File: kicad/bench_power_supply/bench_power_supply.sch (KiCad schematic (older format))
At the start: 0 parts

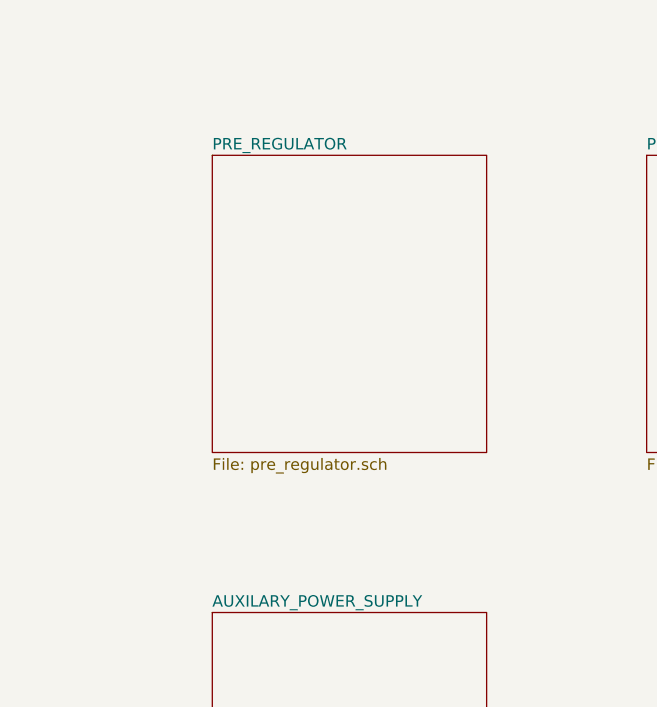
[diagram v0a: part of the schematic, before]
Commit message: Added pre-regulator connector hlabels
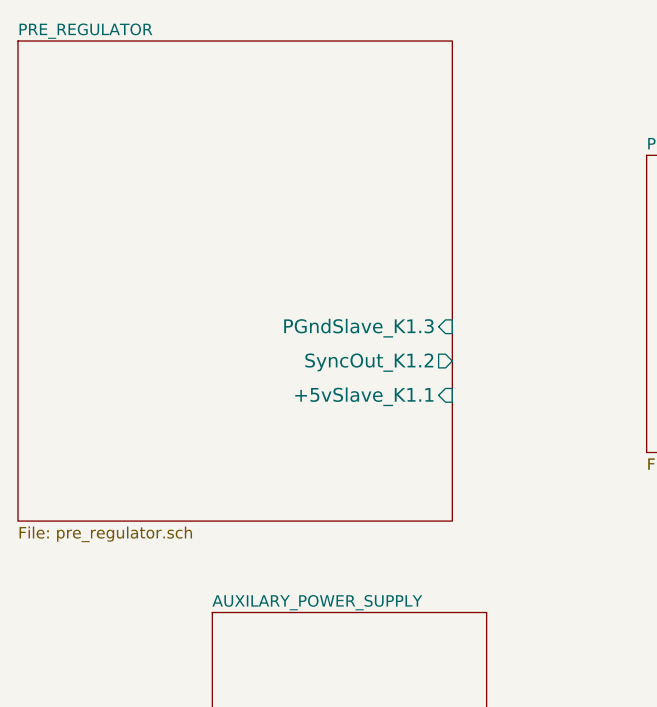
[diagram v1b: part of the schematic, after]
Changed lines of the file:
@@
 Sheet 1 5
 Title "ROOT"
-Date "9 feb 2016"
+Date "15 feb 2016"
 Rev ""
 Comp ""
@@
 Comment4 ""
 $EndDescr
-$Sheet
-S 1700 1150 1200 1300
-U 56BA34F4
-F0 "PRE_REGULATOR" 50
-F1 "pre_regulator.sch" 50
-$EndSheet
 $Sheet
 S 3600 1150 1200 1300
@@
 F1 "digital_control.sch" 50
 $EndSheet
+$Sheet
+S 850  650  1900 2100
+U 56BA34F4
+F0 "PRE_REGULATOR" 50
+F1 "pre_regulator.sch" 50
+F2 "+5vSlave_K1.1" I R 2750 2200 60
+F3 "SyncOut_K1.2" O R 2750 2050 60
+F4 "PGndSlave_K1.3" I R 2750 1900 60
+$EndSheet
 $EndSCHEMATC

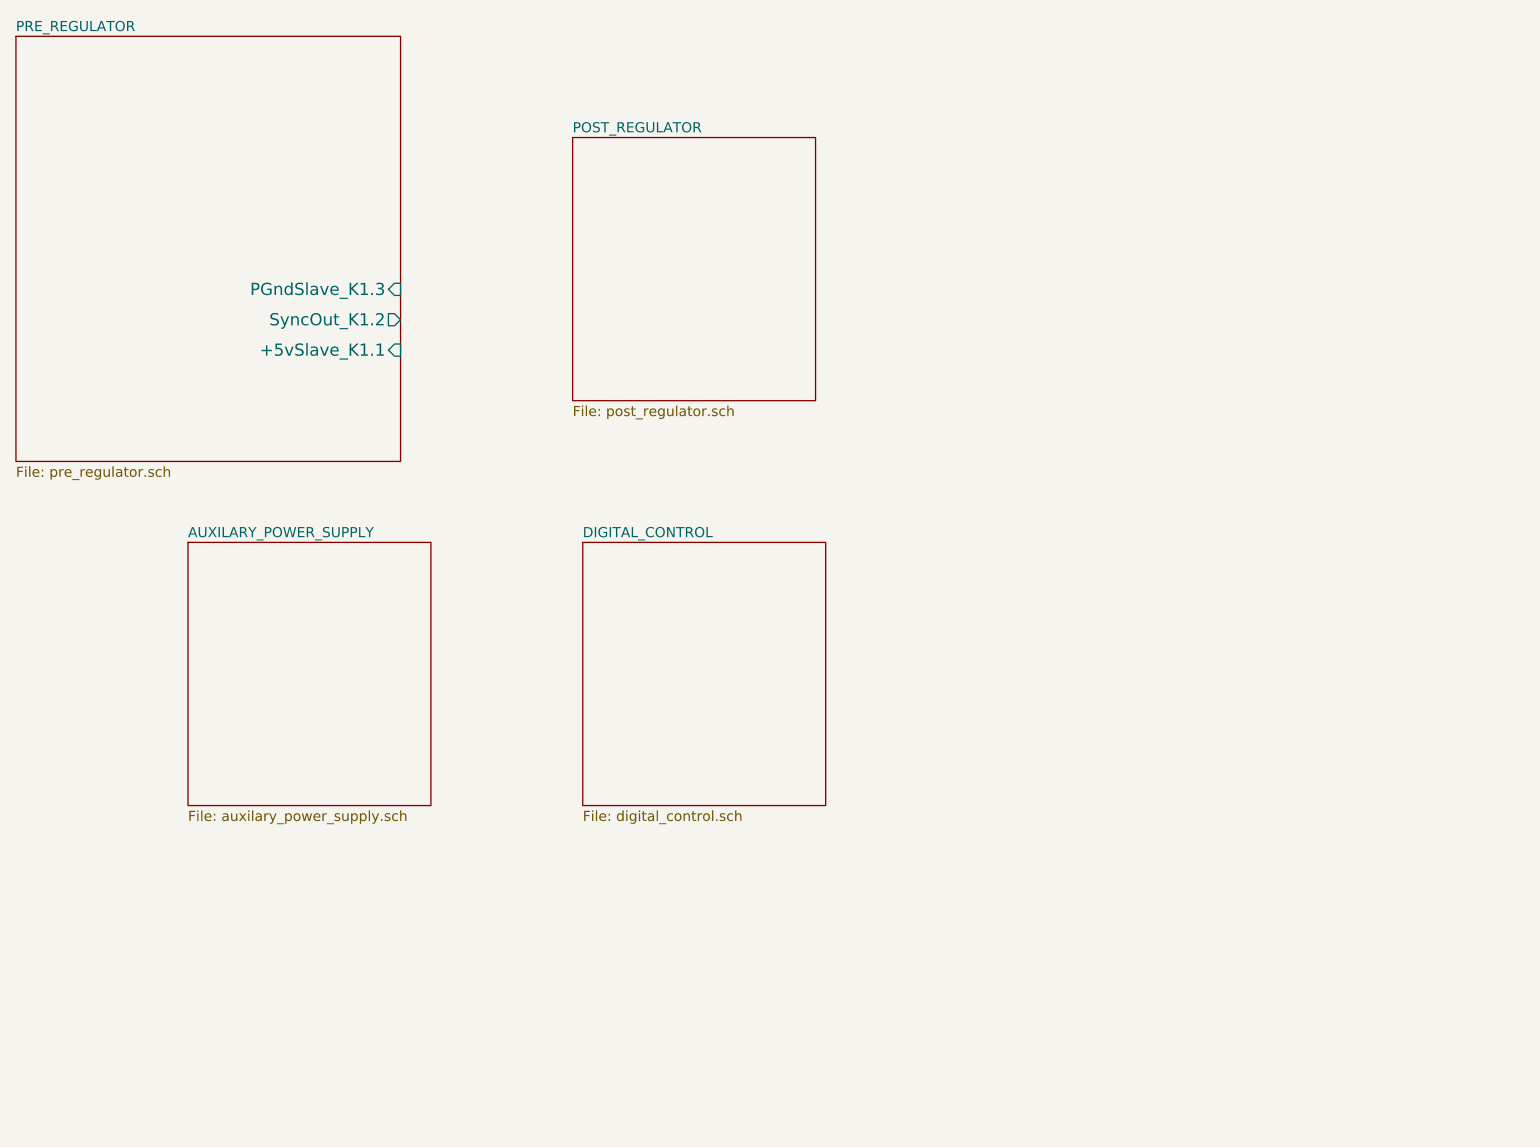
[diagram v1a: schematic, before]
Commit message: Added hlabels to pre-regulator
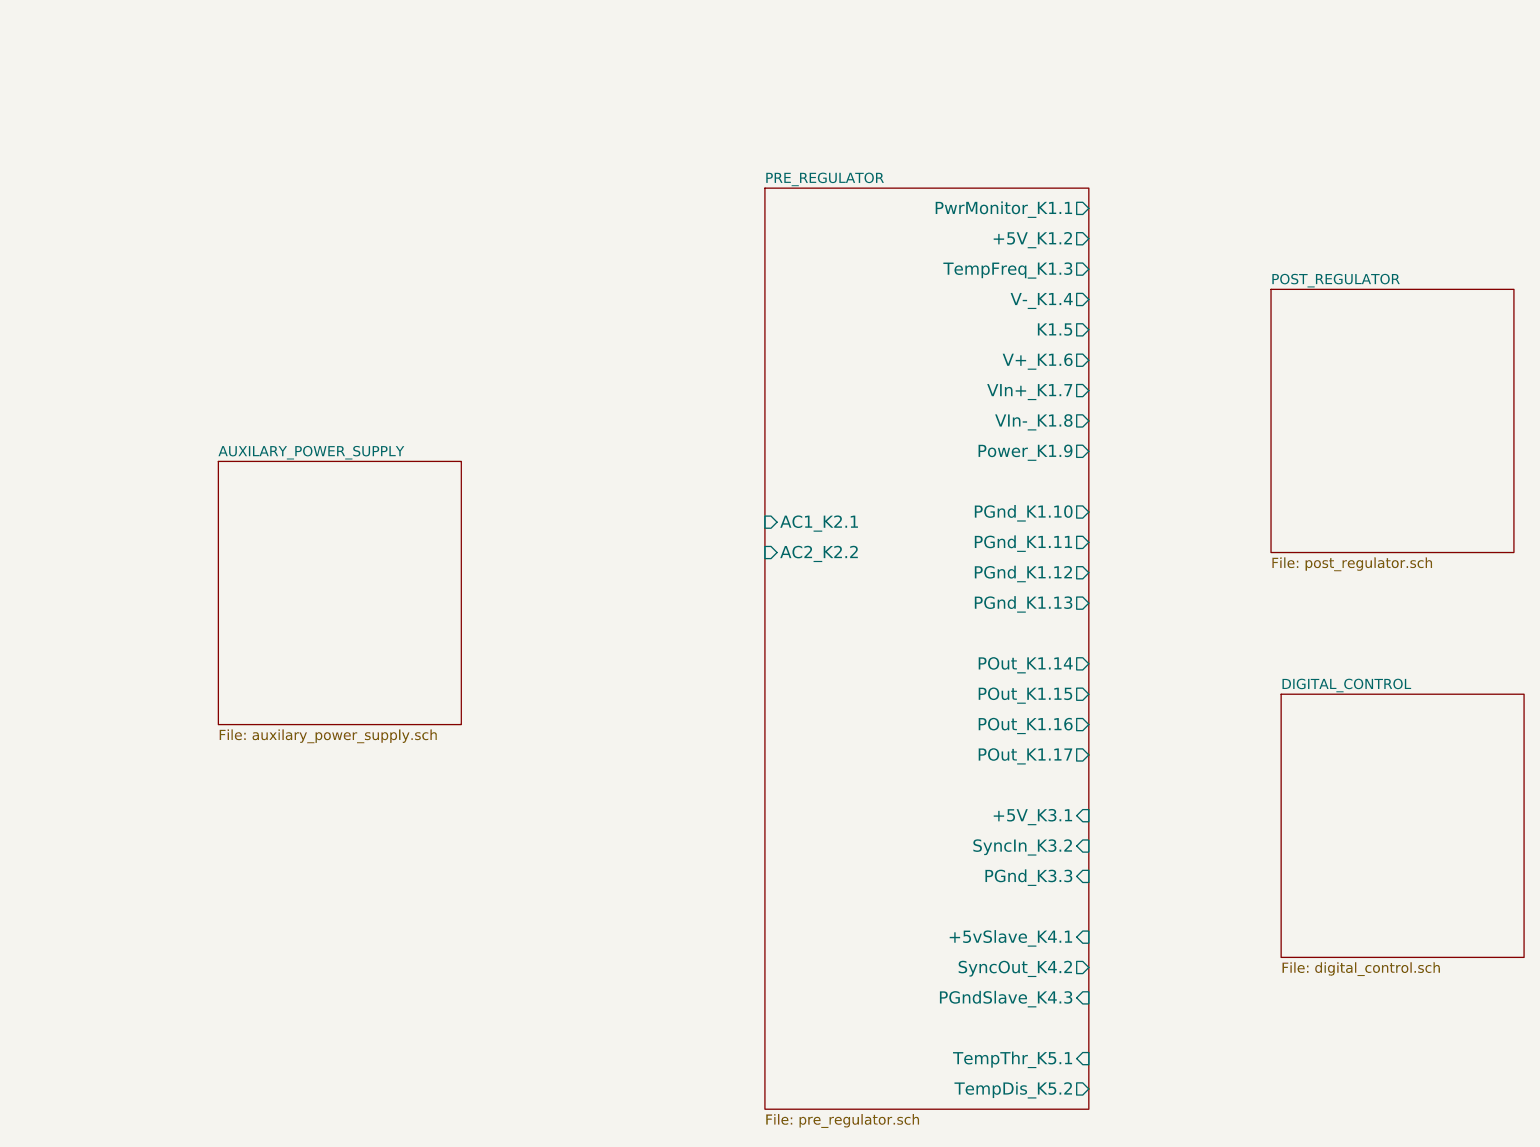
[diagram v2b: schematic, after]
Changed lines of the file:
@@
 $EndDescr
 $Sheet
-S 3600 1150 1200 1300
+S 7050 1900 1200 1300
 U 56BA3538
 F0 "POST_REGULATOR" 50
@@
 $EndSheet
 $Sheet
-S 1700 3150 1200 1300
+S 1850 2750 1200 1300
 U 56BA3567
 F0 "AUXILARY_POWER_SUPPLY" 50
@@
 $EndSheet
 $Sheet
-S 3650 3150 1200 1300
+S 7100 3900 1200 1300
 U 56BA363F
 F0 "DIGITAL_CONTROL" 50
@@
 $EndSheet
 $Sheet
-S 850  650  1900 2100
+S 4550 1400 1600 4550
 U 56BA34F4
 F0 "PRE_REGULATOR" 50
 F1 "pre_regulator.sch" 50
-F2 "+5vSlave_K1.1" I R 2750 2200 60
-F3 "SyncOut_K1.2" O R 2750 2050 60
-F4 "PGndSlave_K1.3" I R 2750 1900 60
+F2 "+5V_K3.1" I R 6150 4500 60
+F3 "SyncIn_K3.2" I R 6150 4650 60
+F4 "PGnd_K3.3" I R 6150 4800 60
+F5 "TempThr_K5.1" I R 6150 5700 60
+F6 "TempDis_K5.2" O R 6150 5850 60
+F7 "+5V_K1.2" O R 6150 1650 60
+F8 "PwrMonitor_K1.1" O R 6150 1500 60
+F9 "TempFreq_K1.3" O R 6150 1800 60
+F10 "POut_K1.15" O R 6150 3900 60
+F11 "POut_K1.14" O R 6150 3750 60
+F12 "POut_K1.17" O R 6150 4200 60
+F13 "POut_K1.16" O R 6150 4050 60
+F14 "PGnd_K1.11" O R 6150 3150 60
+F15 "PGnd_K1.10" O R 6150 3000 60
+F16 "PGnd_K1.13" O R 6150 3450 60
+F17 "PGnd_K1.12" O R 6150 3300 60
+F18 "Power_K1.9" O R 6150 2700 60
+F19 "V-_K1.4" O R 6150 1950 60
+F20 "V+_K1.6" O R 6150 2250 60
+F21 "VIn+_K1.7" O R 6150 2400 60
+F22 "VIn-_K1.8" O R 6150 2550 60
+F23 "+5vSlave_K4.1" I R 6150 5100 60
+F24 "SyncOut_K4.2" O R 6150 5250 60
+F25 "PGndSlave_K4.3" I R 6150 5400 60
+F26 "K1.5" O R 6150 2100 60
+F27 "AC1_K2.1" I L 4550 3050 60
+F28 "AC2_K2.2" I L 4550 3200 60
 $EndSheet
 $EndSCHEMATC

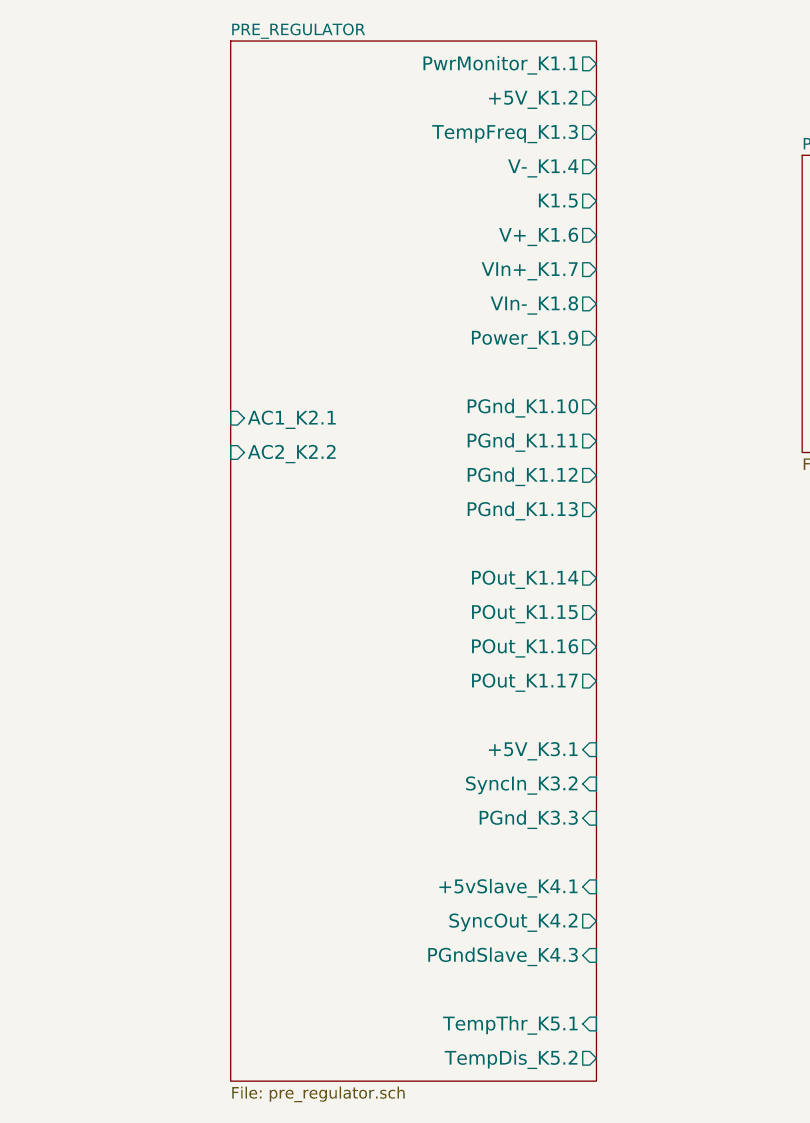
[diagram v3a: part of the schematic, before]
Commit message: Split pre-regulator into two new schemas. Previous pre_regulator.sch has been renamed to pre_regulator_module.
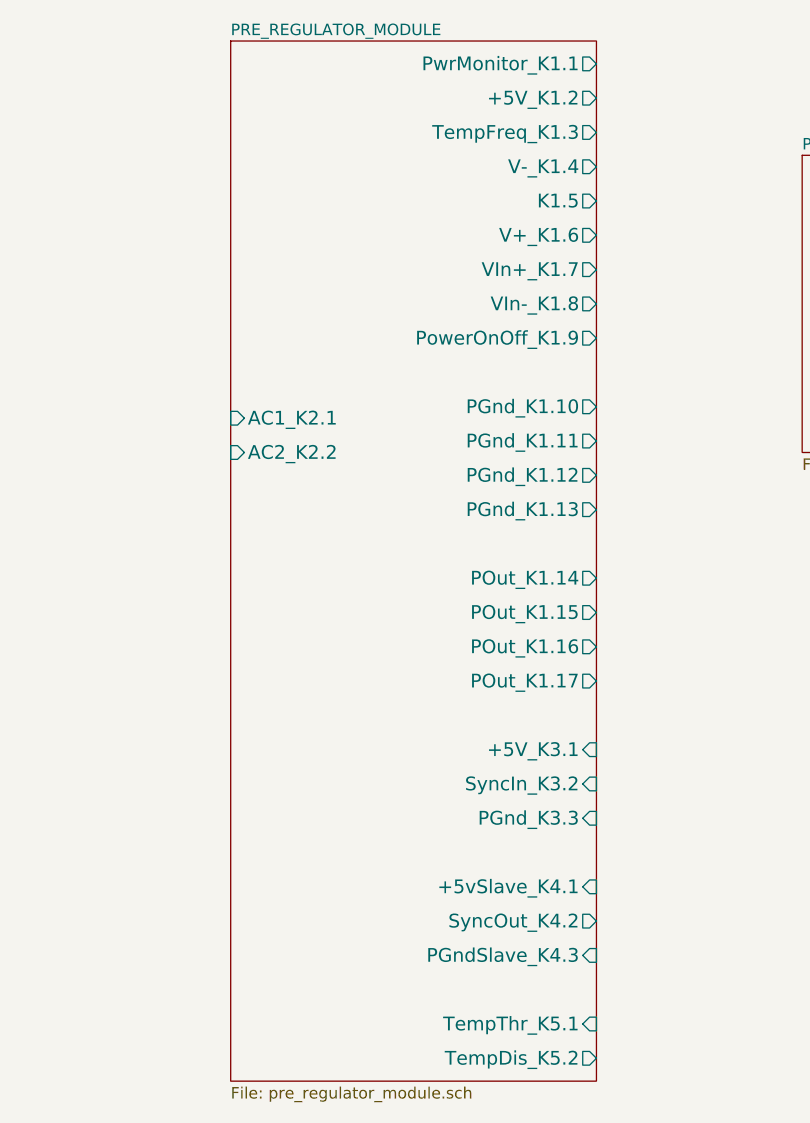
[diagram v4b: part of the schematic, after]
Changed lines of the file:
@@
 $Descr A4 11693 8268
 encoding utf-8
-Sheet 1 5
+Sheet 1 7
 Title "ROOT"
-Date "10 mar 2016"
+Date "24 apr 2016"
 Rev ""
 Comp ""
@@
 S 4550 1400 1600 4550
 U 56BA34F4
-F0 "PRE_REGULATOR" 50
-F1 "pre_regulator.sch" 50
+F0 "PRE_REGULATOR_MODULE" 50
+F1 "pre_regulator_module.sch" 50
 F2 "+5V_K3.1" I R 6150 4500 60
 F3 "SyncIn_K3.2" I R 6150 4650 60
@@
 F16 "PGnd_K1.13" O R 6150 3450 60
 F17 "PGnd_K1.12" O R 6150 3300 60
-F18 "Power_K1.9" O R 6150 2700 60
+F18 "PowerOnOff_K1.9" O R 6150 2700 60
 F19 "V-_K1.4" O R 6150 1950 60
 F20 "V+_K1.6" O R 6150 2250 60

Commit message: added files from mint
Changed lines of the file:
@@
 EESchema Schematic File Version 2
+LIBS:bench_power_supply-rescue
 LIBS:my_library
 LIBS:power
@@
 LIBS:memory
 LIBS:xilinx
-LIBS:special
 LIBS:microcontrollers
 LIBS:dsp
@@
 LIBS:my_transistors
 LIBS:bench_power_supply-cache
-EELAYER 27 0
+EELAYER 25 0
 EELAYER END
 $Descr A4 11693 8268
 encoding utf-8
-Sheet 1 7
+Sheet 1 9
 Title "ROOT"
-Date "24 apr 2016"
+Date "11 may 2016"
 Rev ""
 Comp ""
@@
 S 4550 1400 1600 4550
 U 56BA34F4
-F0 "PRE_REGULATOR_MODULE" 50
-F1 "pre_regulator_module.sch" 50
-F2 "+5V_K3.1" I R 6150 4500 60
+F0 "POWER_MODULE" 50
+F1 "power_module.sch" 50
+F2 "+5V_K3.1" O R 6150 4500 60
 F3 "SyncIn_K3.2" I R 6150 4650 60
 F4 "PGnd_K3.3" I R 6150 4800 60
 F5 "TempThr_K5.1" I R 6150 5700 60
 F6 "TempDis_K5.2" O R 6150 5850 60
-F7 "+5V_K1.2" O R 6150 1650 60
-F8 "PwrMonitor_K1.1" O R 6150 1500 60
-F9 "TempFreq_K1.3" O R 6150 1800 60
-F10 "POut_K1.15" O R 6150 3900 60
-F11 "POut_K1.14" O R 6150 3750 60
-F12 "POut_K1.17" O R 6150 4200 60
-F13 "POut_K1.16" O R 6150 4050 60
-F14 "PGnd_K1.11" O R 6150 3150 60
-F15 "PGnd_K1.10" O R 6150 3000 60
-F16 "PGnd_K1.13" O R 6150 3450 60
-F17 "PGnd_K1.12" O R 6150 3300 60
-F18 "PowerOnOff_K1.9" O R 6150 2700 60
-F19 "V-_K1.4" O R 6150 1950 60
-F20 "V+_K1.6" O R 6150 2250 60
-F21 "VIn+_K1.7" O R 6150 2400 60
-F22 "VIn-_K1.8" O R 6150 2550 60
+F7 "+5V_K2.2" O R 6150 1650 60
+F8 "PwrMonitor_K2.1" O R 6150 1500 60
+F9 "TempFreq_K2.3" O R 6150 1800 60
+F10 "POut_K2.15" O R 6150 3900 60
+F11 "POut_K2.14" O R 6150 3750 60
+F12 "POut_K2.17" O R 6150 4200 60
+F13 "POut_K2.16" O R 6150 4050 60
+F14 "PGnd_K2.11" O R 6150 3150 60
+F15 "PGnd_K2.10" O R 6150 3000 60
+F16 "PGnd_K2.13" O R 6150 3450 60
+F17 "PGnd_K2.12" O R 6150 3300 60
+F18 "PowerOnOff_K2.9" O R 6150 2700 60
+F19 "V-_K2.4" O R 6150 1950 60
+F20 "V+_K2.6" O R 6150 2250 60
+F21 "+9V_K2.7" O R 6150 2400 60
+F22 "-9V_K2.8" O R 6150 2550 60
 F23 "+5vSlave_K4.1" I R 6150 5100 60
 F24 "SyncOut_K4.2" O R 6150 5250 60
 F25 "PGndSlave_K4.3" I R 6150 5400 60
-F26 "K1.5" O R 6150 2100 60
-F27 "AC1_K2.1" I L 4550 3050 60
-F28 "AC2_K2.2" I L 4550 3200 60
+F26 "K2.5" O R 6150 2100 60
+F27 "AC1_K1.1" I L 4550 3050 60
+F28 "AC2_K1.2" I L 4550 3200 60
+F29 "DcOut_K2.18" O R 6150 4350 60
 $EndSheet
 $EndSCHEMATC
